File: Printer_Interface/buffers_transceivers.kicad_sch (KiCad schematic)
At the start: 17 parts, among them U1 74FCT16245, U2 74HCT245, U3 74HCT1G32, U4 74HCT1G32, U5 74HCT1G32, U6 74HCT1G32

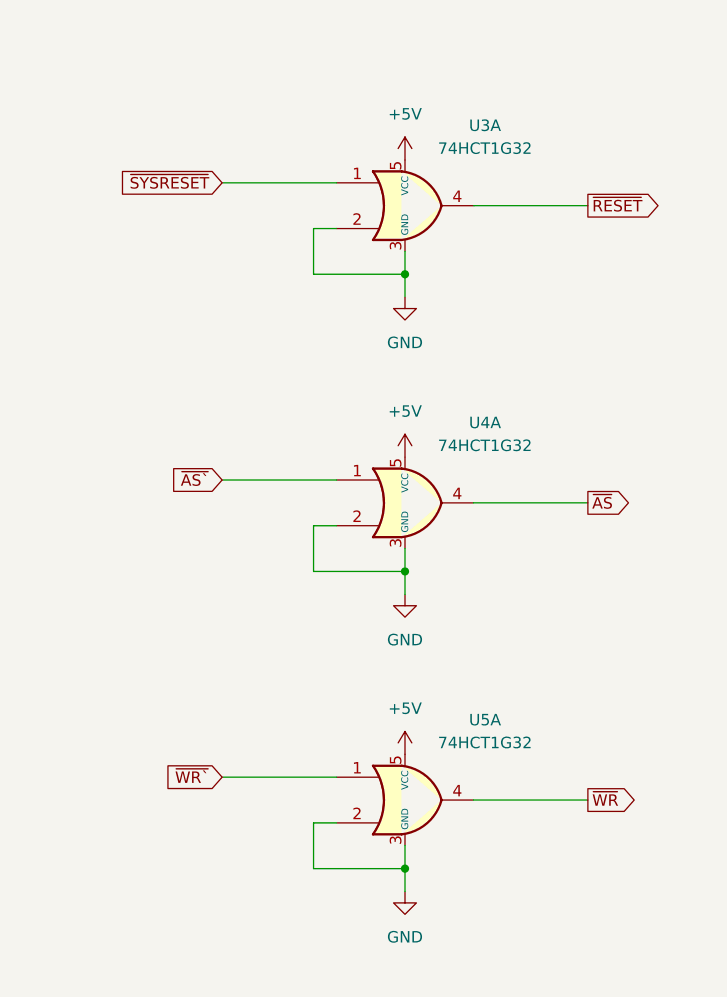
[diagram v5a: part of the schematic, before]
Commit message: Incorporate symbol fixes
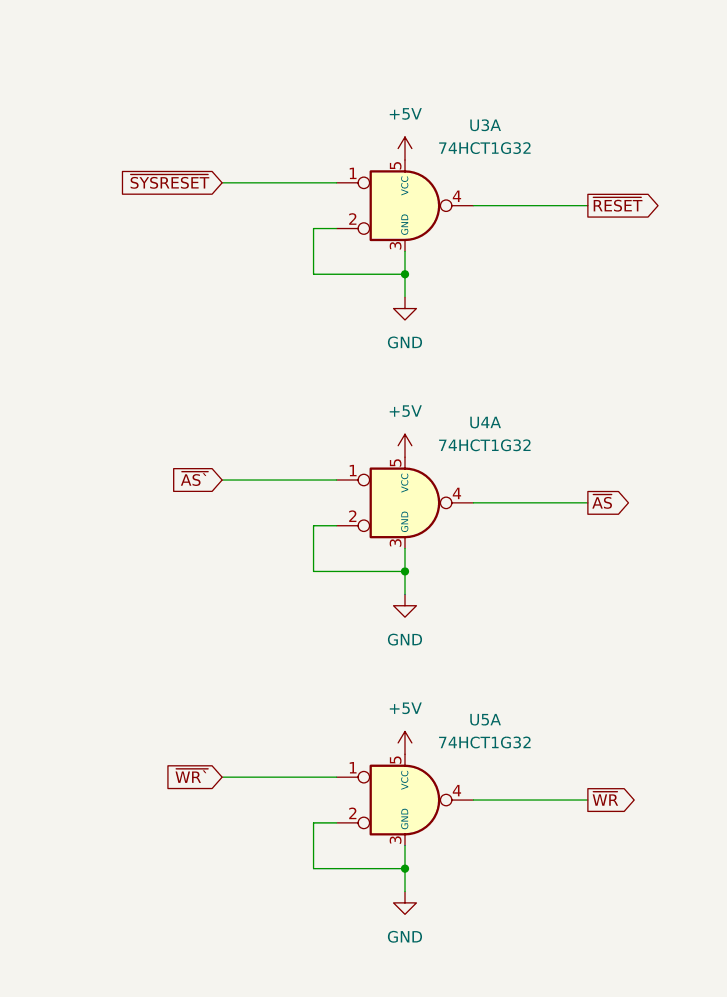
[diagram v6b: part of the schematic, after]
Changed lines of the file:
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@@
 		(at 238.76 38.1 0)
 		(unit 1)
+		(convert 2)
 		(exclude_from_sim no)
 		(in_bom yes)
@@
 		(at 238.76 71.12 0)
 		(unit 1)
+		(convert 2)
 		(exclude_from_sim no)
 		(in_bom yes)
@@
 		(at 238.76 104.14 0)
 		(unit 1)
-		(exclude_from_sim no)
-		(in_bom yes)
+		(convert 2)
+		(exclude_from_sim no)
+		(in_bom yes)
